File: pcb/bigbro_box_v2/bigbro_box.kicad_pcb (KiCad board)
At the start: 2 copper layers, 100 x 58 mm, 43 parts, among them J1 Current Sense, J2 Display, J3 Mains, J4 Debug, J5 RFID, J6 Relay, K1 G5LE-1, Q1 MMBT3904, Q2 MMBT3904, Q3 BSS138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

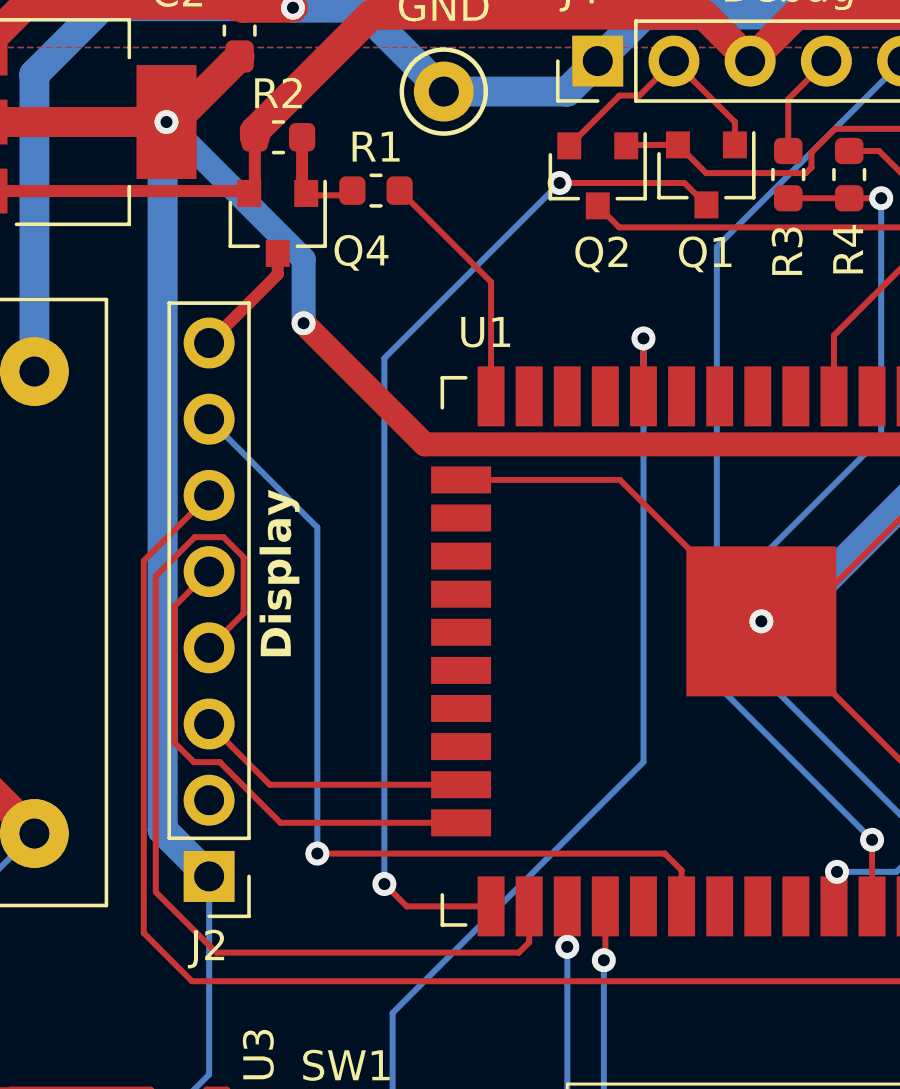
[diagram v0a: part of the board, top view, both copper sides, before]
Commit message: Add extension connector.
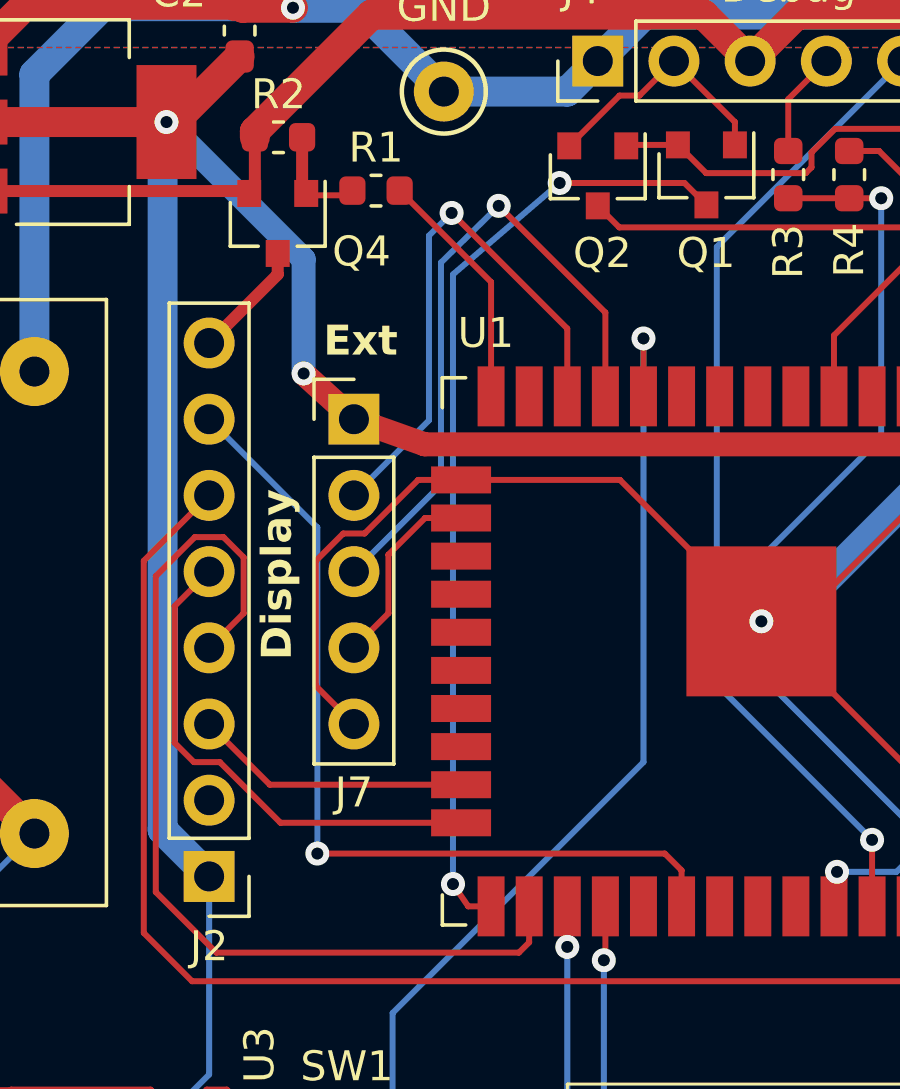
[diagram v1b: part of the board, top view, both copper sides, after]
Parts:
- added J7: Ext, Connector_PinHeader_2.54mm:PinHeader_1x05_P2.54mm_Vertical, F.Cu at (120.7, 72.4)
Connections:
- U1 pad 11: unconnected-(U1-IO26-Pad11) -> Ext2
- U1 pad 12: unconnected-(U1-IO27-Pad12) -> Ext3
- U1 pad 16: unconnected-(U1-IO13-Pad16) -> Ext1
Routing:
- net Ext2: track 0.00 -> 22.0 mm, vias 0 -> 1
- net Ext3: track 0.00 -> 18.5 mm, vias 0 -> 1
- net GND: track 259.5 -> 271.4 mm
- net Ext1: track 0.00 -> 6.51 mm
- net /~{BOOT}: track 34.8 -> 31.9 mm
- net +3V3: track 111.6 -> 112.3 mm
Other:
- board text added: "Ext"

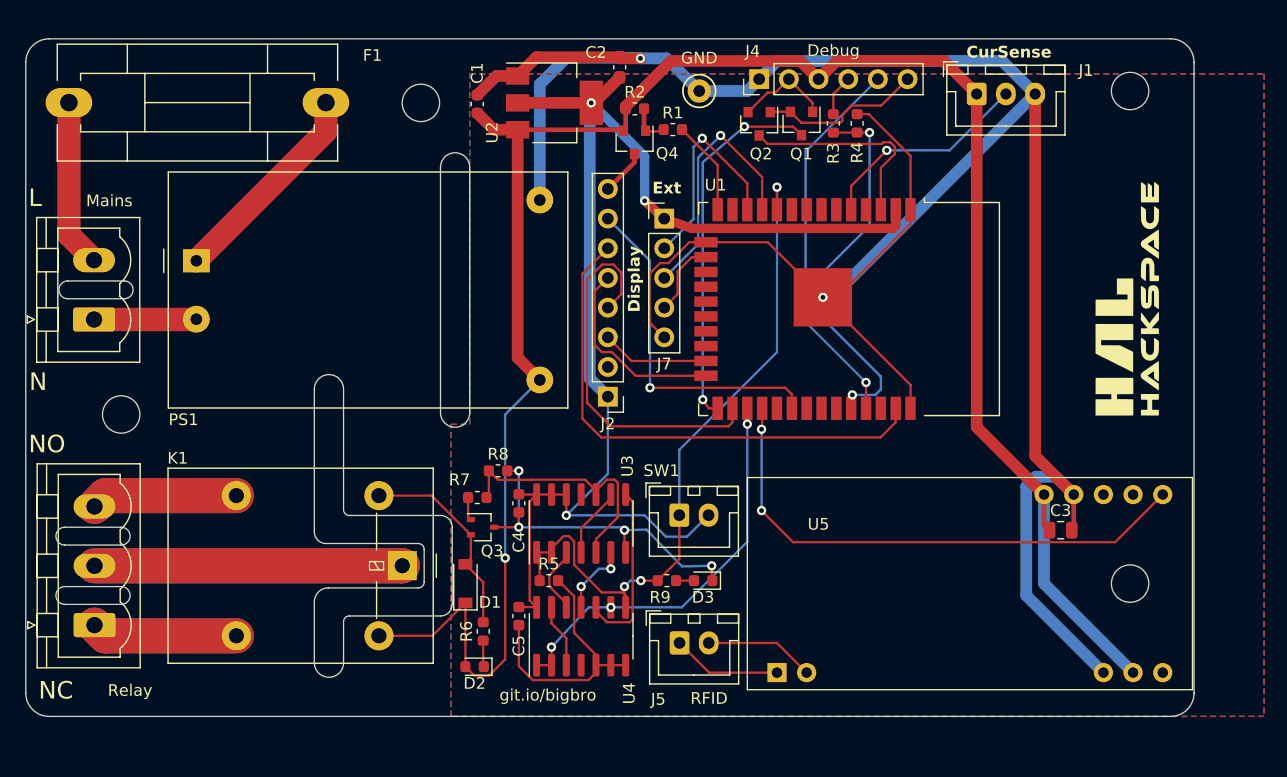
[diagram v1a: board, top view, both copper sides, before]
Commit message: Fill zones.
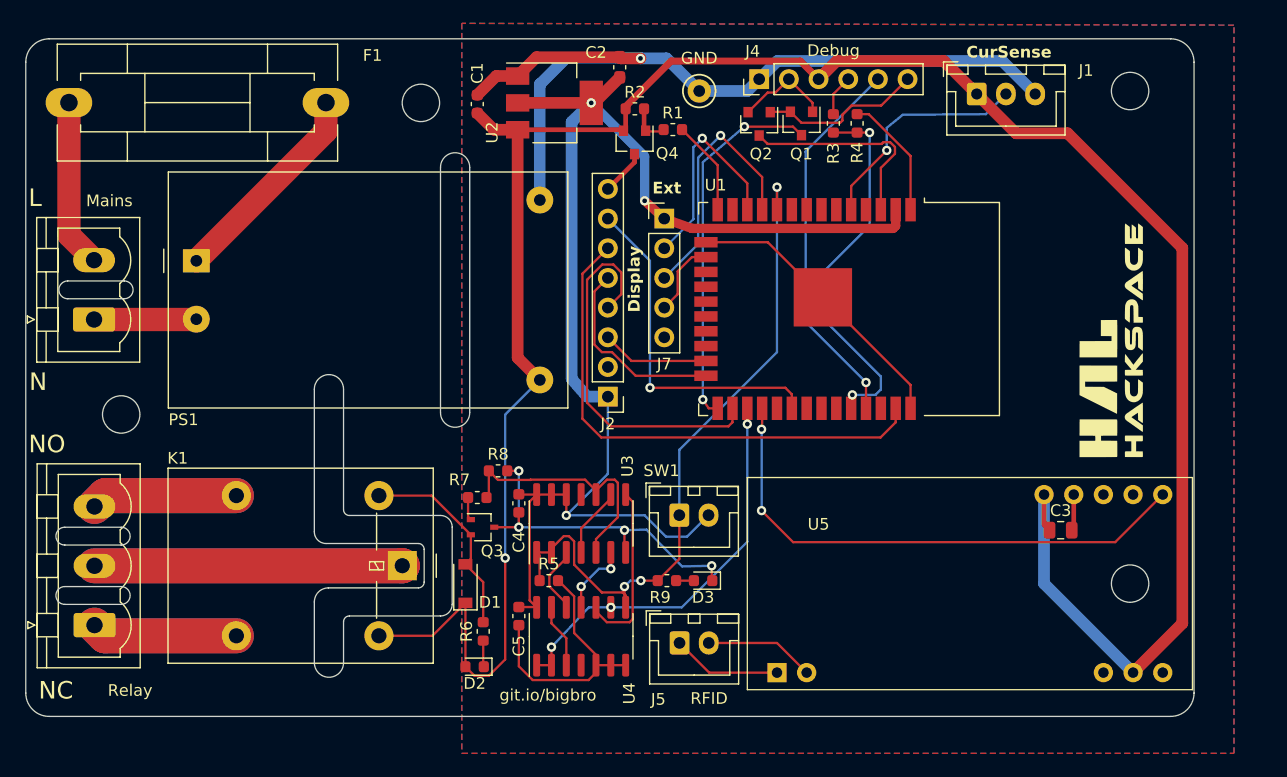
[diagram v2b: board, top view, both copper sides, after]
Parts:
- moved G*** 3.81 mm to (158.9, 82.8)
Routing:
- net GND: track 271.4 -> 164.6 mm, vias 6 -> 5
- net +5V: track 173.5 -> 197.8 mm
- net +3V3: track 112.3 -> 114.6 mm
- net /CurrentSense: track 18.5 -> 19.6 mm

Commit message: Remove solder mask on high-current traces.
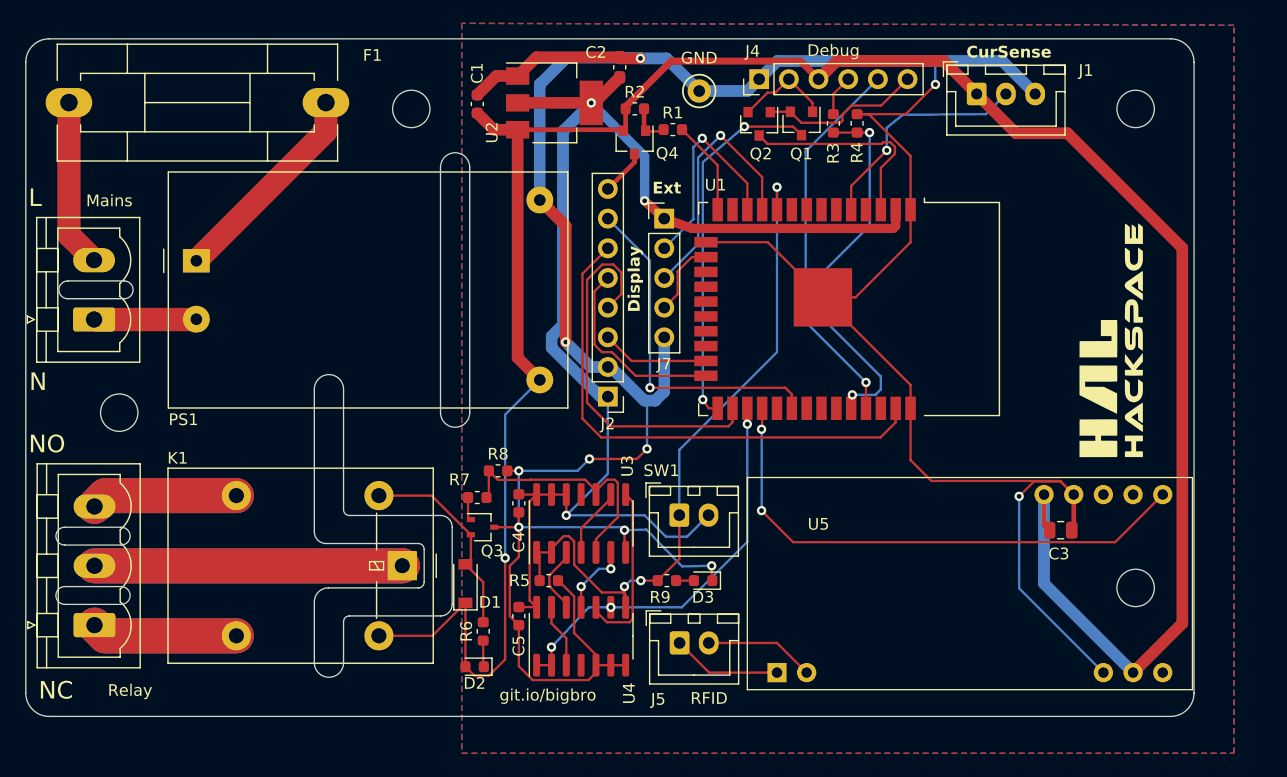
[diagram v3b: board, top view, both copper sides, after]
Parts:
- moved H3 1.60 mm to (161.0, 63.0)
- moved H2 0.97 mm to (99.0, 63.0)
- moved H4 0.60 mm to (161.0, 104.0)
- moved H1 0.23 mm to (74.0, 89.0)
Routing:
- net GND: track 164.6 -> 282.3 mm, vias 5 -> 10
- net +3V3: track 114.6 -> 115.4 mm

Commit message: Clarify connector labels.
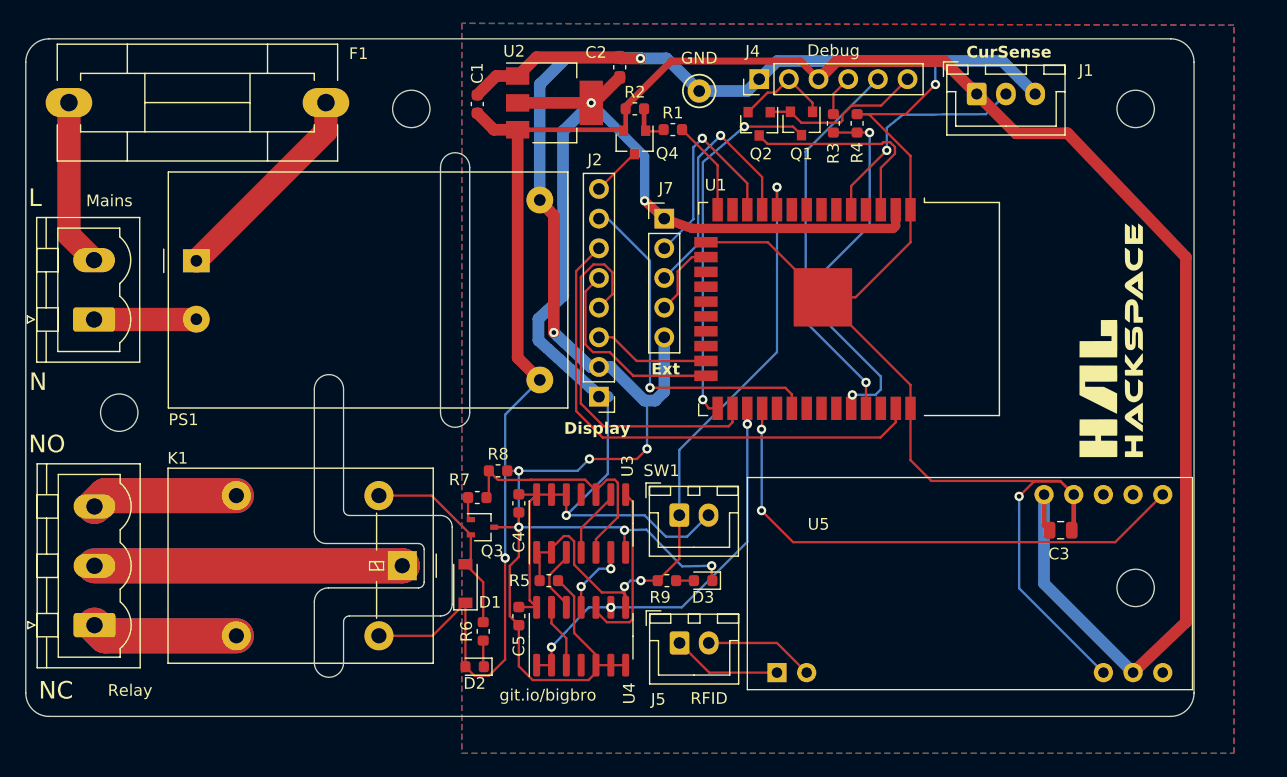
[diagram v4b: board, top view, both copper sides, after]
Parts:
- moved J2 0.76 mm to (115.1, 87.6)
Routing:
- net +3V3: track 115.4 -> 116.5 mm
- net Display_CS: track 9.24 -> 10.00 mm
- net Display_A0: track 16.8 -> 17.6 mm
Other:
- outline, holes or cut-outs redrawn

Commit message: Order.
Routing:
- net GND: track 282.3 -> 282.8 mm
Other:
- board text added: "•"
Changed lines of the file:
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@@
     (pad "1" thru_hole circle (at 0 0) (size 2 2) (drill 1) (layers "*.Cu" "*.Mask")
       (net 2 "GND") (pinfunction "1") (pintype "passive"))
-    (model "${KICAD6_3DMODEL_DIR}/TestPoint.3dshapes/TestPoint_Keystone_5000-5004_Miniature.wrl"
+    (model "${KIPRJMOD}/lib/3D/TestPoint_Loop_D2.60mm_Drill0.9mm_Beaded.step"
       (offset (xyz 0 0 0))
       (scale (xyz 1 1 1))
@@
     (effects (font (size 1 1) (thickness 0.18) bold) (justify left bottom))
   )
+  (gr_text "•" (at 126.8476 60.9092) (layer "F.SilkS")
+    (effects (font (size 1 1) (thickness 0.15)) (justify left bottom mirror))
+  )
   (gr_text "N" (at 67.056 86.36) (layer "F.SilkS")
     (effects (font (size 1.5 1.5) (thickness 0.3)))
@@
     (effects (font (size 1.5 1.5) (thickness 0.3)))
   )
+  (gr_text "•" (at 119.634 70.5104) (layer "F.SilkS")
+    (effects (font (size 1 1) (thickness 0.15)) (justify left bottom mirror))
+  )
+  (gr_text "•" (at 145.542 58.3692) (layer "F.SilkS")
+    (effects (font (size 1 1) (thickness 0.15)) (justify left bottom mirror))
+  )
   (gr_text "Display" (at 112.0648 90.932) (layer "F.SilkS")
     (effects (font (size 1 1) (thickness 0.18) bold) (justify left bottom))
   )
+  (gr_text "•" (at 118.0084 89.5604) (layer "F.SilkS")
+    (effects (font (size 1 1) (thickness 0.15)) (justify left bottom mirror))
+  )
   (gr_text "GND" (at 122.0724 59.2328) (layer "F.SilkS")
     (effects (font (size 1 1) (thickness 0.15)) (justify left bottom))
@@
   (segment (start 153.162 103.632) (end 160.782 111.252) (width 1) (layer "B.Cu") (net 1))
   (segment (start 107.0356 101.4476) (end 107.0356 89.1644) (width 0.2) (layer "B.Cu") (net 1))
-  (segment (start 141.732 88.628) (end 141.732 93.061822) (width 0.2) (layer "F.Cu") (net 2))
   (segment (start 108.204 97.536) (end 108.204 98.806) (width 0.2) (layer "F.Cu") (net 2))
   (segment (start 118.3132 92.964) (end 119.1768 92.1004) (width 0.2) (layer "F.Cu") (net 2))
@@
   (segment (start 112.938 104.722604) (end 112.938 107.858) (width 0.2) (layer "F.Cu") (net 2))
   (segment (start 137.16 63.449) (end 138.155223 63.449) (width 0.2) (layer "F.Cu") (net 2))
-  (segment (start 154.5336 94.8436) (end 155.702 96.012) (width 0.2) (layer "F.Cu") (net 2))
   (segment (start 106.2735 60.184) (end 108.102 60.184) (width 1) (layer "F.Cu") (net 2))
   (segment (start 129.517 74.413) (end 134.232 79.128) (width 0.2) (layer "F.Cu") (net 2))
   (segment (start 124.222 74.413) (end 129.517 74.413) (width 0.2) (layer "F.Cu") (net 2))
-  (segment (start 141.732 93.061822) (end 143.513778 94.8436) (width 0.2) (layer "F.Cu") (net 2))
   (segment (start 108.204 110.701396) (end 109.391604 111.889) (width 0.2) (layer "F.Cu") (net 2))
   (segment (start 109.7125 58.5735) (end 108.102 60.184) (width 1) (layer "F.Cu") (net 2))
@@
   (segment (start 118.618 58.674) (end 116.9405 58.674) (width 1) (layer "F.Cu") (net 2))
   (segment (start 141.3258 63.449) (end 143.8656 60.9092) (width 0.2) (layer "F.Cu") (net 2))
-  (segment (start 143.513778 94.8436) (end 154.5336 94.8436) (width 0.2) (layer "F.Cu") (net 2))
   (segment (start 124.714 103.327) (end 124.765 103.378) (width 0.2) (layer "F.Cu") (net 2))
   (segment (start 111.2012 72.136) (end 110 70.8) (width 1) (layer "F.Cu") (net 2))
   (segment (start 108.204 107.188) (end 108.204 110.701396) (width 0.2) (layer "F.Cu") (net 2))
+  (segment (start 154.5336 94.8436) (end 155.702 96.012) (width 0.2) (layer "F.Cu") (net 2))
   (segment (start 114.808 110.614) (end 116.078 110.614) (width 0.2) (layer "F.Cu") (net 2))
+  (segment (start 141.732 88.628) (end 141.7828 94.0308) (width 0.2) (layer "F.Cu") (net 2))
   (segment (start 111.2012 82.1436) (end 111.2012 72.136) (width 1) (layer "F.Cu") (net 2))
   (segment (start 109.391604 111.889) (end 114.171 111.889) (width 0.2) (layer "F.Cu") (net 2))
@@
   (segment (start 111.557 103.378) (end 111.593396 103.378) (width 0.2) (layer "F.Cu") (net 2))
   (segment (start 107.429 102.121) (end 108.204 101.346) (width 0.2) (layer "F.Cu") (net 2))
+  (segment (start 141.7828 94.0308) (end 142.6464 94.8436) (width 0.2) (layer "F.Cu") (net 2))
+  (segment (start 142.6464 94.8436) (end 154.5336 94.8436) (width 0.2) (layer "F.Cu") (net 2))
   (segment (start 107.2135 93.98) (end 108.204 93.98) (width 0.2) (layer "F.Cu") (net 2))
   (segment (start 116.078 110.614) (end 117.348 110.614) (width 0.2) (layer "F.Cu") (net 2))
@@
       (pts
         (xy 154.7876 94.476)
-        (xy 143.2876 94.476)
-        (xy 143.3892 65.786)
+        (xy 142.932 94.4252)
+        (xy 143.0336 65.7352)
         (xy 154.8892 65.786)
       )

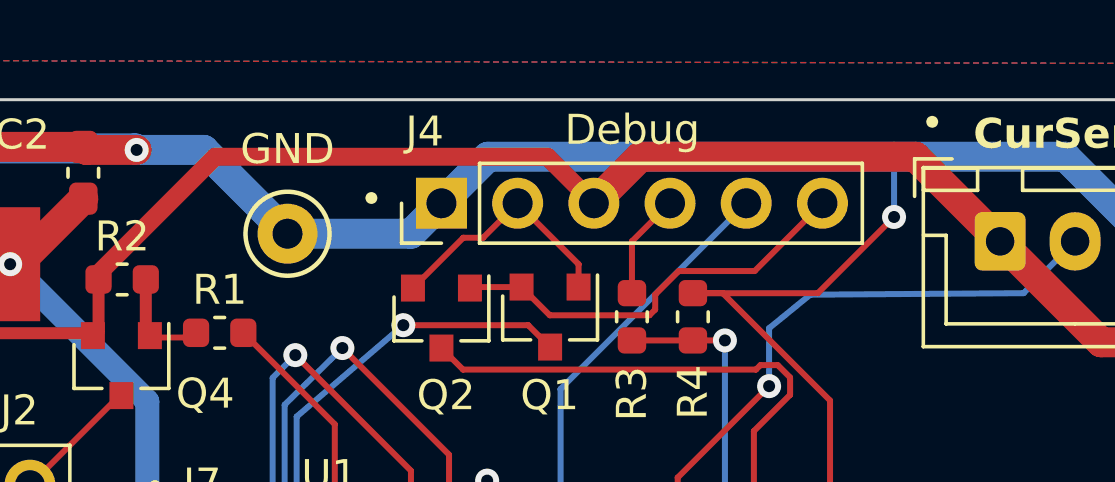
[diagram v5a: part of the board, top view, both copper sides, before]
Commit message: Improve debug connector labels.
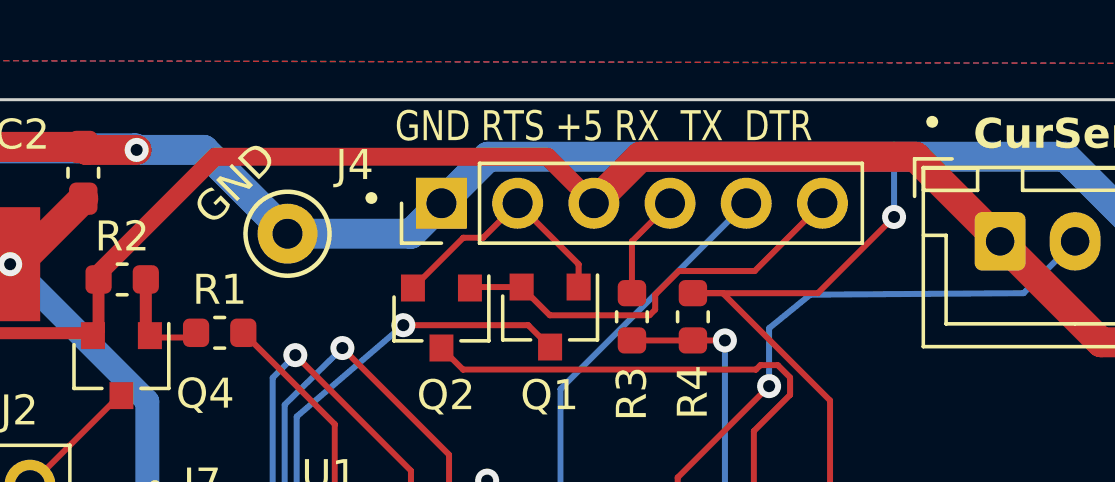
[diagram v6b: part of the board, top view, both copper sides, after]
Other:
- board text added: "GND RTS +5 RX TX DTR"
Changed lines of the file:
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@@
-(kicad_pcb (version 20221018) (generator pcbnew)
+(kicad_pcb (version 20230410) (generator pcbnew)
   (general
     (thickness 1.6)
@@
       (hpglpenspeed 20)
       (hpglpendiameter 15.000000)
+      (pdf_front_fp_property_popups true)
+      (pdf_back_fp_property_popups true)
       (dxfpolygonmode true)
       (dxfimperialunits true)
@@
     (property "ki_keywords" "connector")
     (attr through_hole)
-    (fp_text reference "J4" (at 2.3876 -0.5588 -180) (layer "F.SilkS")
+    (fp_text reference "J4" (at 1.27 -2.8956 -180) (layer "F.SilkS")
       (effects (font (size 1 1) (thickness 0.15)))
     )
-    (fp_text value "Debug" (at 2.445145 6.360625) (layer "F.SilkS")
+    (fp_text value "Debug" (at 2.445145 6.360625) (layer "F.SilkS") hide
       (effects (font (size 1 1) (thickness 0.18)))
     )
@@
     (effects (font (size 1 1) (thickness 0.15)) (justify left bottom mirror))
   )
+  (gr_text "GND RTS +5 RX  TX  DTR" (at 127.2286 58.4708) (layer "F.SilkS")
+    (effects (font (size 1 0.8) (thickness 0.15)) (justify left bottom))
+  )
   (gr_text "N" (at 67.056 86.36) (layer "F.SilkS")
     (effects (font (size 1.5 1.5) (thickness 0.3)))
@@
     (effects (font (size 1 1) (thickness 0.15)) (justify left bottom mirror))
   )
-  (gr_text "GND" (at 122.0724 59.2328) (layer "F.SilkS")
+  (gr_text "GND" (at 121.2088 61.3156 45) (layer "F.SilkS")
     (effects (font (size 1 1) (thickness 0.15)) (justify left bottom))
   )
